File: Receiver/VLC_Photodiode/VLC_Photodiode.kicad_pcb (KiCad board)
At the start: 2 copper layers, 30 x 40 mm, 7 parts, among them J1 Screw_Terminal_01x02, J2 RF3-05-T-00-50-G, J3 RF3-05-T-00-50-G, J4 RF3-05-T-00-50-G

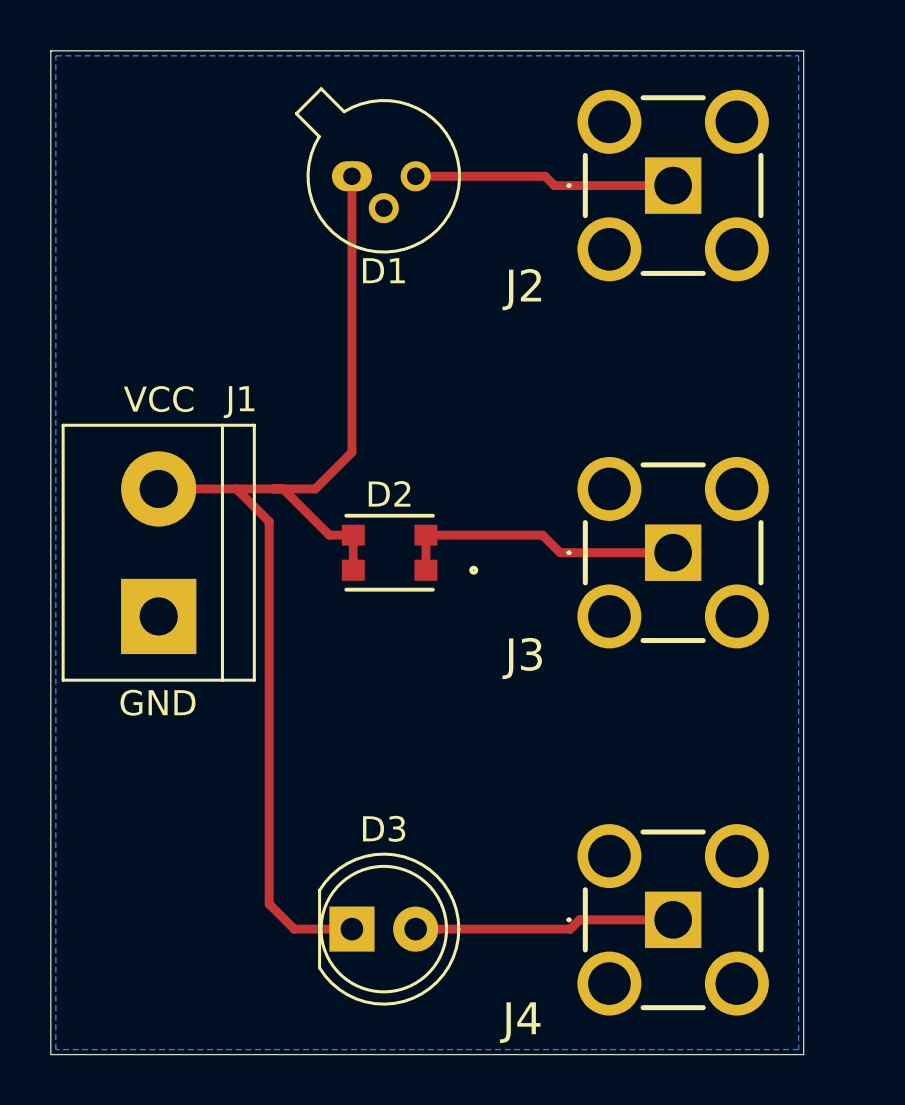
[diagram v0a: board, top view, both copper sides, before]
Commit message: Push v2 according to Issue#1
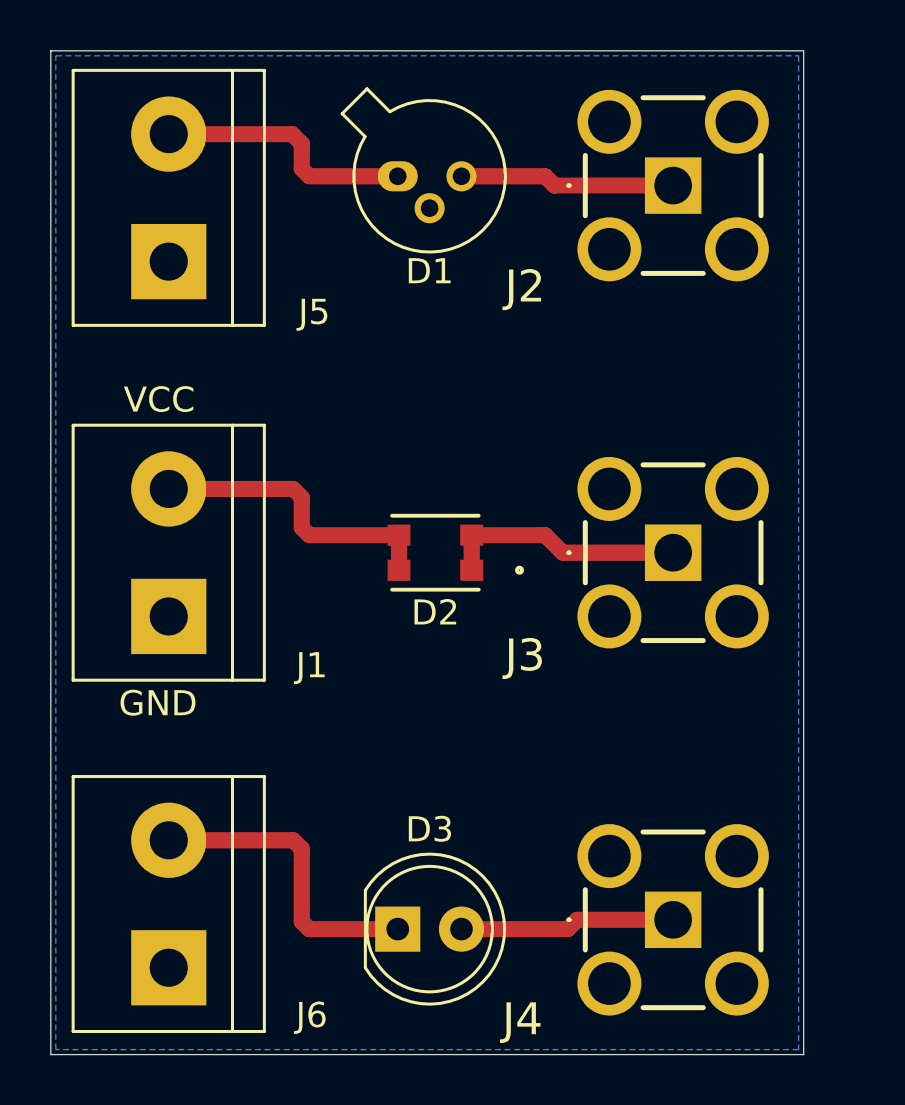
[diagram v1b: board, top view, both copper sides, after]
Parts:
- added J5: Screw_Terminal_01x02, TerminalBlock:TerminalBlock_bornier-2_P5.08mm, F.Cu at (104.7, 68.4)
- added J6: Screw_Terminal_01x02, TerminalBlock:TerminalBlock_bornier-2_P5.08mm, F.Cu at (104.7, 96.5)
- moved D1 1.83 mm to (113.8, 65.0)
- moved D2 1.83 mm to (115.3, 80.0)
- moved D3 1.83 mm to (113.8, 95.0)
- moved J1 0.40 mm to (104.7, 82.5)
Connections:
- D2 pad 3: Net-(D1-K) -> Net-(J1-Pin_2)
- D2 pad 4: Net-(D1-K) -> Net-(J1-Pin_2)
- D3 pad 1: Net-(D1-K) -> Net-(D3-K)
- J1 pad 2: Net-(D1-K) -> Net-(J1-Pin_2)
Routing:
- net Net-(D1-K): track 45.4 -> 10.4 mm
- net Net-(D3-K): track 0.00 -> 12.3 mm
- net Net-(J1-Pin_2): track 0.00 -> 12.0 mm
- net Net-(J3-In): track 11.5 -> 9.71 mm
- net Net-(D3-A): track 10.4 -> 8.59 mm
- net Net-(D1-A): track 10.4 -> 8.59 mm
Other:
- board text added: "Copper Thickness = 1oz (35um) Dielectric = FR4 Dielectric Thickness = 1.2mm"

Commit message: Version Sma Edge
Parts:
- J2, J3, J4: value RF3-05-T-00-50-G -> SMA H; footprint Lumicom_Photodiode:RF305T0050G -> Connector_Coaxial:SMA_Samtec_SMA-J-P-H-ST-EM1_EdgeMount
- moved J4 2.38 mm to (122.4, 94.4)
- moved J2 2.37 mm to (122.4, 65.6)
- moved J3 2.36 mm to (122.4, 80.0)
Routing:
- net GND: track 0.00 -> 9.60 mm, vias 0 -> 6
- net Net-(J3-In): track 9.71 -> 7.35 mm
- net Net-(D1-A): track 8.59 -> 6.32 mm
- net Net-(D3-A): track 8.59 -> 6.33 mm
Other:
- board size 30 x 40 mm -> 25 x 40 mm

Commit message: v3 according to Issue #1
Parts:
- moved D2 0.70 mm to (115.3, 80.7)
- moved D3 0.62 mm to (113.8, 94.4)
- moved D1 0.60 mm to (113.8, 65.6)
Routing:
- net Net-(D3-K): track 12.3 -> 11.5 mm
- net Net-(J1-Pin_2): track 12.0 -> 12.6 mm
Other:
- board text added: "PDB-C154"

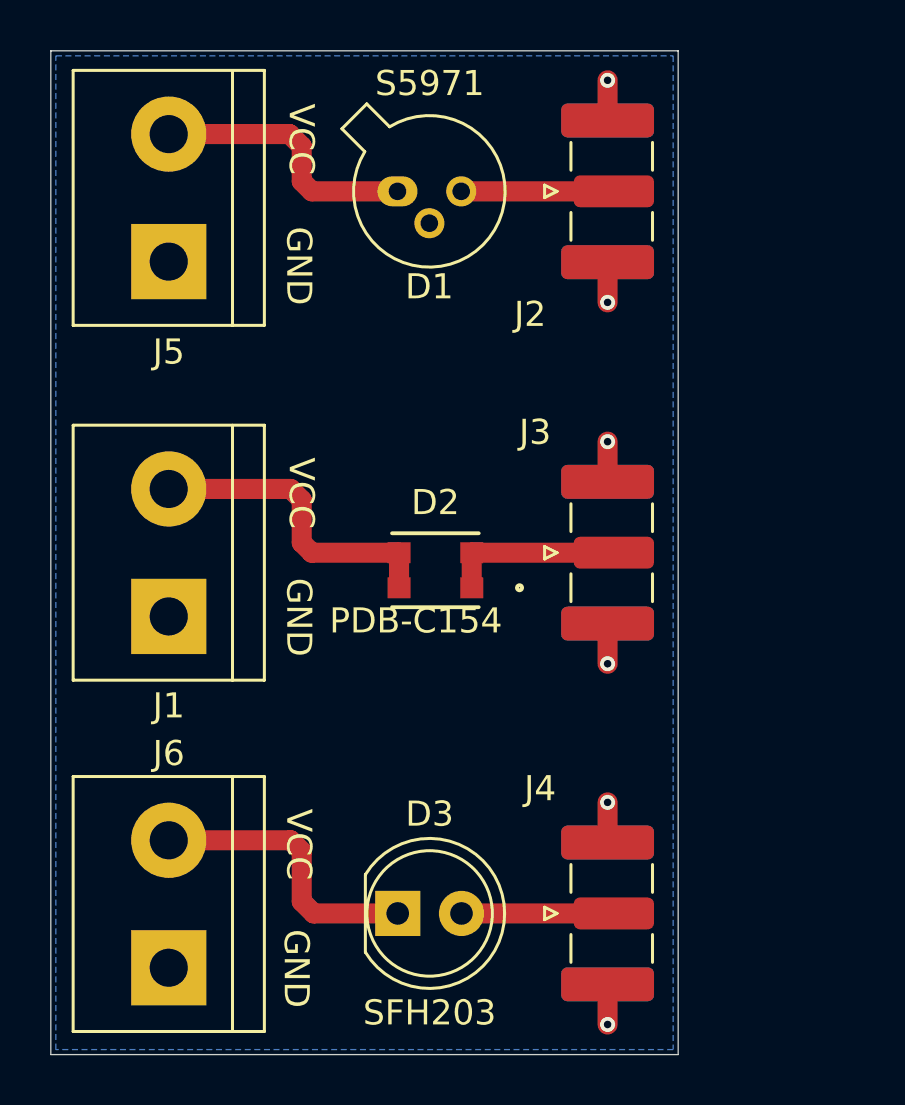
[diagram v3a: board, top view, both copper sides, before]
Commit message: LED uploaded, PD reworked
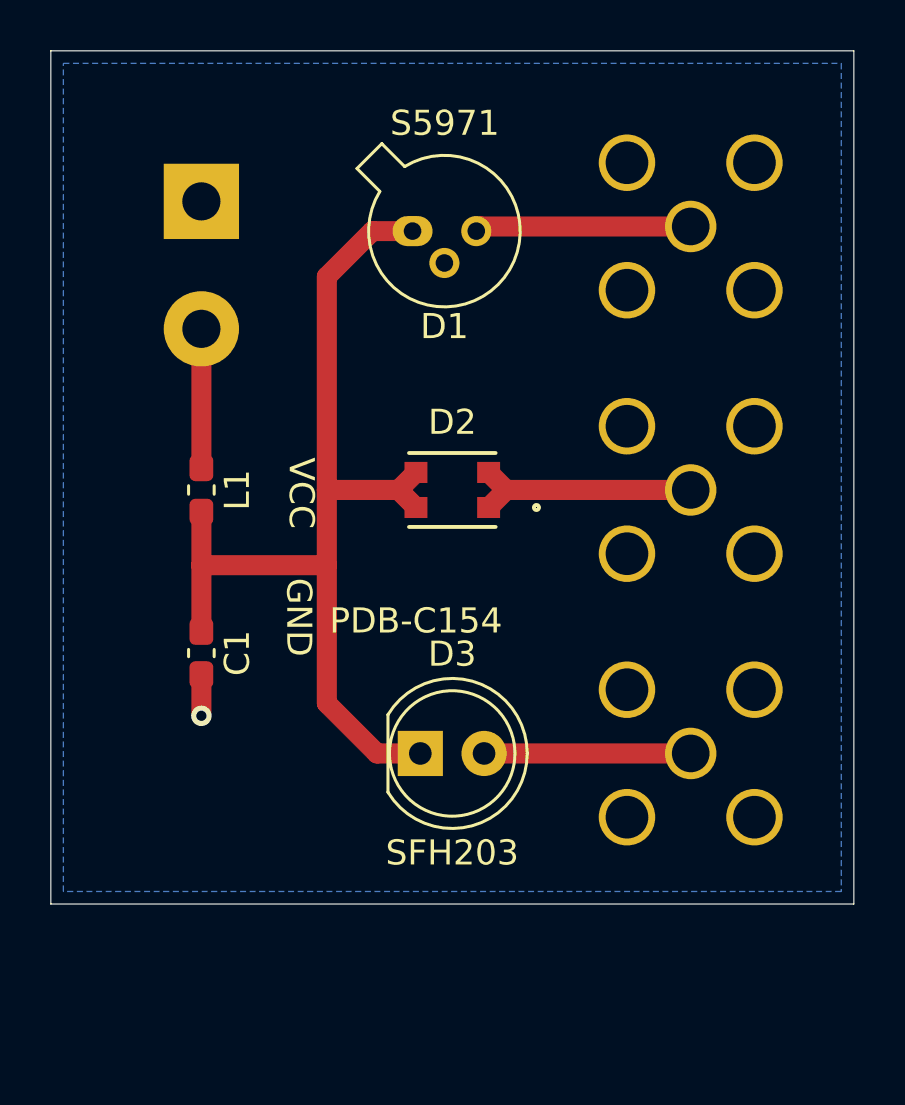
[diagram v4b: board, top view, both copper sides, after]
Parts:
- removed J1, J6: Screw_Terminal_01x02, TerminalBlock:TerminalBlock_bornier-2_P5.08mm
- added C1: 10uF, Capacitor_SMD:C_0603_1608Metric_Pad1.08x0.95mm_HandSolder, F.Cu at (106.0, 84.0)
- added L1: BLM18BA100SN1D, Inductor_SMD:L_0603_1608Metric_Pad1.05x0.95mm_HandSolder, F.Cu at (106.0, 77.5)
- J2, J3, J4: value SMA H -> RFPC-SMA28-F; footprint Connector_Coaxial:SMA_Samtec_SMA-J-P-H-ST-EM1_EdgeMount -> Lumicom_Photodiode:RFPC-SMA28-F; moved to B.Cu
- J5: moved to B.Cu
- moved J4 7.07 mm to (125.5, 88.0), turned to 180 degrees
- moved D3 6.44 mm to (114.7, 88.0)
- moved J3 3.95 mm to (125.5, 77.5), turned to 180 degrees
- moved J2 3.37 mm to (125.5, 67.0), turned to 180 degrees
- moved D2 3.27 mm to (116.0, 77.5)
- moved J5 2.73 mm to (106.0, 66.0), turned to -90 degrees
- moved D1 1.69 mm to (114.4, 67.2)
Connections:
- D2 pad 3: Net-(J1-Pin_2) -> Net-(D1-K)
- D2 pad 4: Net-(J1-Pin_2) -> Net-(D1-K)
- D3 pad 1: Net-(D3-K) -> Net-(D1-K)
- J5 pad 2: Net-(D1-K) -> Net-(J5-Pin_2)
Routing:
- net Net-(D1-K): track 10.9 -> 40.3 mm
- net Net-(J1-Pin_2): track 12.6 -> 0.00 mm
- net Net-(D3-K): track 11.5 -> 0.00 mm
- net GND: track 9.60 -> 1.64 mm, vias 6 -> 1
- net Net-(J5-Pin_2): track 0.00 -> 5.55 mm
- net Net-(D1-A): track 6.08 -> 8.62 mm
- net Net-(J3-In): track 7.06 -> 9.33 mm
- net Net-(D3-A): track 6.07 -> 8.23 mm
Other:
- board size 25 x 40 mm -> 32 x 34 mm
- board text added: "AP"
- board text added: "H"
- board text added: "O"

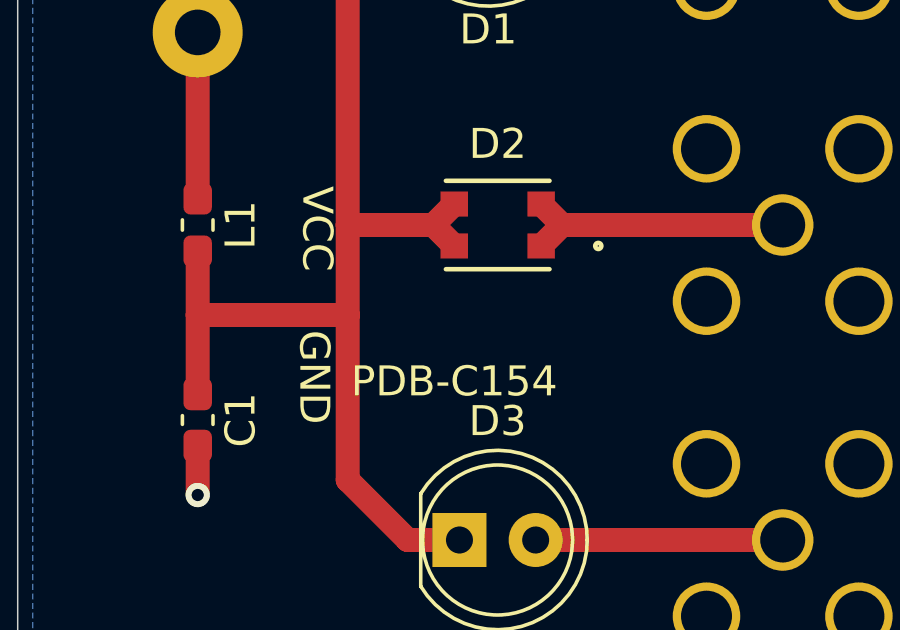
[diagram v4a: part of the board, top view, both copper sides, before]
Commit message: PD reworked, LED uploaded
PD reworked
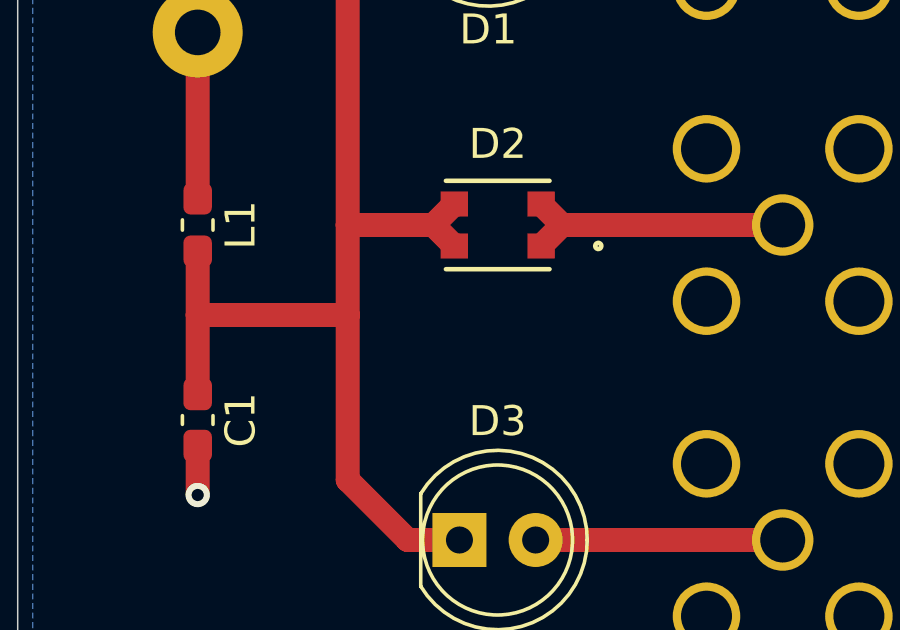
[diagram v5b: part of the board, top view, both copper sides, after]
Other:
- board text removed: "PDB-C154"
